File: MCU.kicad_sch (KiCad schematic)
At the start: 16 parts, among them SW1 KMR221NGLFS, U1 STM32L432KCUx

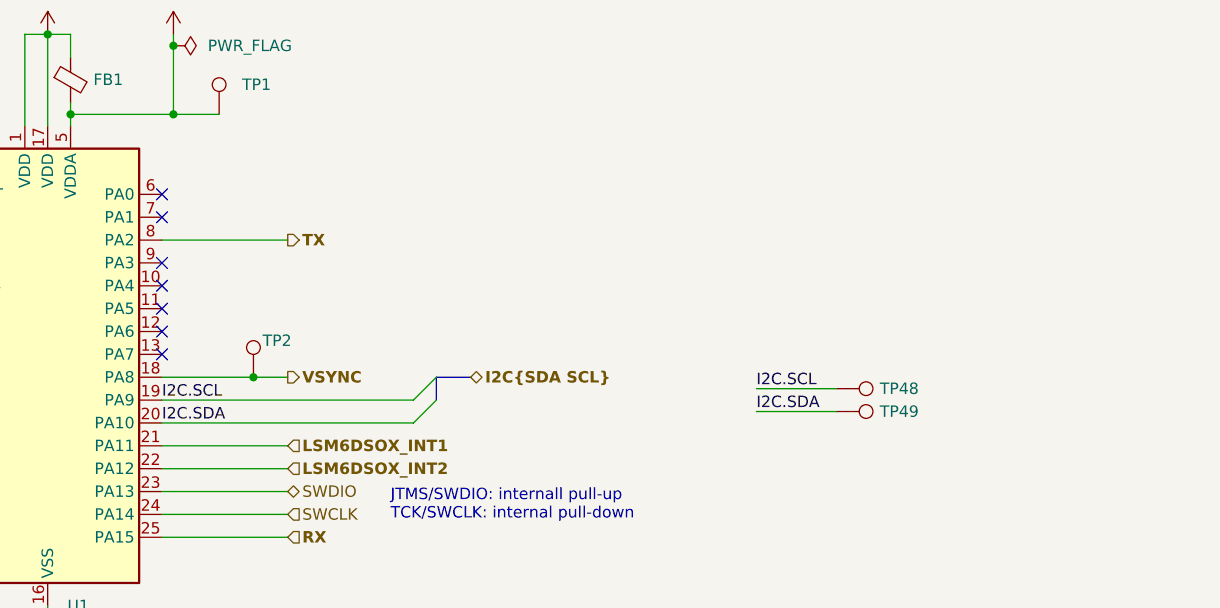
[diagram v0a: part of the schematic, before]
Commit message: Changed PUs for I2C and added TPs.
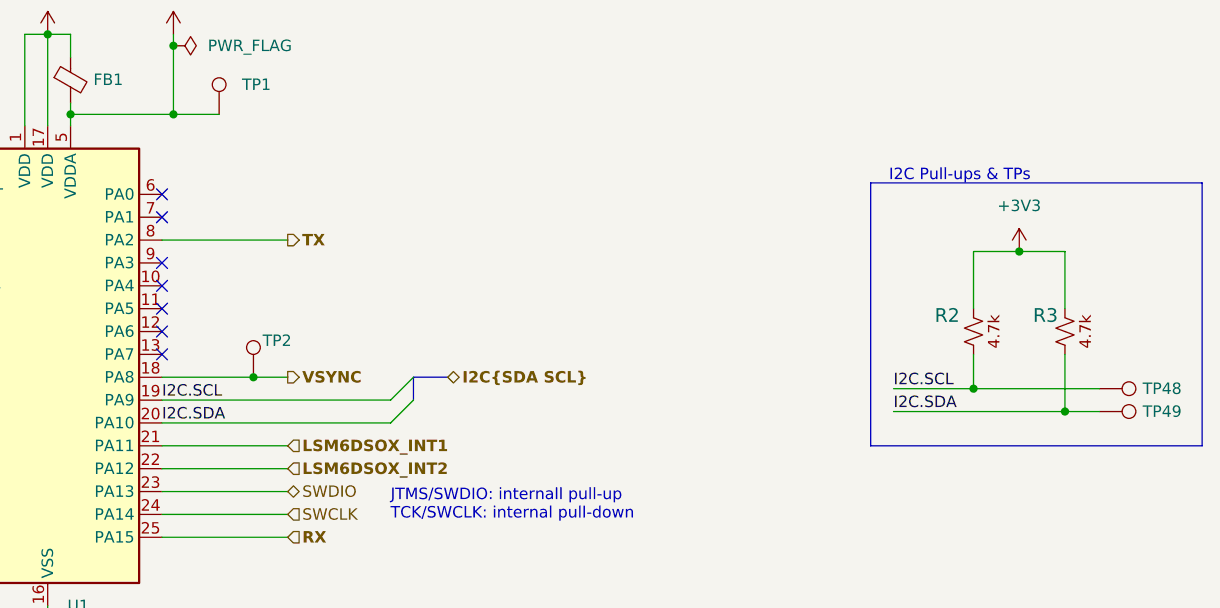
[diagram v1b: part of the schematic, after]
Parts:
- added R2, R3: CRGCQ0805F4K7, Hourglass_footprint_library:CRGCQ0805F4K7, symbol Hourglass_symbol_library:CRGCQ0805F4K7
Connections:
- net +3V3: now also R2.2, R3.2
- net I2C.SCL: now also R2.1
- net I2C.SDA: now also R3.1
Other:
- note added: "I2C Pull-ups & TPs"
- moved on the sheet: TP48, TP49

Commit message: Re-annotated entire schematic.
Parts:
- renumbered R17 to R1, R1 to R4, TP48 to TP3, TP49 to TP4, TP50 to TP5
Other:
- title: (none) -> Hourglass
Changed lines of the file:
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@@
 	(generator_version "9.0")
 	(paper "A4")
+	(title_block
+		(title "Hourglass")
+		(date "2025-04-23")
+		(rev "01")
+	)
 	(rectangle
 		(start 16.51 53.34)
@@
 		(on_board yes)
 		(dnp no)
-		(property "Reference" "TP48"
+		(property "Reference" "TP3"
 			(at 271.5261 88.9 90)
 			(effects
@@
 			(project "Hourglass_PCBA"
 				(path "/a75630d2-15a7-42bc-8ce0-7846cbd1da6b/c8d454a4-a64d-492c-9043-c9910b58426e"
-					(reference "TP48")
+					(reference "TP3")
 					(unit 1)
 				)
@@
 		(on_board yes)
 		(dnp no)
-		(property "Reference" "TP49"
+		(property "Reference" "TP4"
 			(at 271.5261 91.44 90)
 			(effects
@@
 			(project "Hourglass_PCBA"
 				(path "/a75630d2-15a7-42bc-8ce0-7846cbd1da6b/c8d454a4-a64d-492c-9043-c9910b58426e"
-					(reference "TP49")
+					(reference "TP4")
 					(unit 1)
 				)
@@
 		(dnp no)
 		(fields_autoplaced yes)
-		(property "Reference" "#PWR10"
+		(property "Reference" "#PWR011"
 			(at 149.86 129.54 0)
 			(effects
@@
 			(project ""
 				(path "/a75630d2-15a7-42bc-8ce0-7846cbd1da6b/c8d454a4-a64d-492c-9043-c9910b58426e"
-					(reference "#PWR10")
+					(reference "#PWR011")
 					(unit 1)
 				)
@@
 		(on_board yes)
 		(dnp no)
-		(property "Reference" "R17"
+		(property "Reference" "R1"
 			(at 60.452 66.0398 90)
 			(effects
@@
 			(project ""
 				(path "/a75630d2-15a7-42bc-8ce0-7846cbd1da6b/c8d454a4-a64d-492c-9043-c9910b58426e"
-					(reference "R17")
+					(reference "R1")
 					(unit 1)
 				)
@@
 		(dnp no)
 		(fields_autoplaced yes)
-		(property "Reference" "#PWR03"
+		(property "Reference" "#PWR07"
 			(at 66.04 66.04 0)
 			(effects
@@
 			(project ""
 				(path "/a75630d2-15a7-42bc-8ce0-7846cbd1da6b/c8d454a4-a64d-492c-9043-c9910b58426e"
-					(reference "#PWR03")
+					(reference "#PWR07")
 					(unit 1)
 				)
@@
 		(dnp no)
 		(fields_autoplaced yes)
-		(property "Reference" "#FLG3"
+		(property "Reference" "#FLG01"
 			(at 165.735 50.8 0)
 			(effects
@@
 			(project ""
 				(path "/a75630d2-15a7-42bc-8ce0-7846cbd1da6b/c8d454a4-a64d-492c-9043-c9910b58426e"
-					(reference "#FLG3")
+					(reference "#FLG01")
 					(unit 1)
 				)
@@
 		(on_board yes)
 		(dnp no)
-		(property "Reference" "R1"
+		(property "Reference" "R4"
 			(at 26.416 127.2538 90)
 			(effects
@@
 			(project ""
 				(path "/a75630d2-15a7-42bc-8ce0-7846cbd1da6b/c8d454a4-a64d-492c-9043-c9910b58426e"
-					(reference "R1")
+					(reference "R4")
 					(unit 1)
 				)
@@
 		(dnp no)
 		(fields_autoplaced yes)
-		(property "Reference" "#PWR5"
+		(property "Reference" "#PWR05"
 			(at 149.86 53.34 0)
 			(effects
@@
 			(project ""
 				(path "/a75630d2-15a7-42bc-8ce0-7846cbd1da6b/c8d454a4-a64d-492c-9043-c9910b58426e"
-					(reference "#PWR5")
+					(reference "#PWR05")
 					(unit 1)
 				)
@@
 		(dnp no)
 		(fields_autoplaced yes)
-		(property "Reference" "#PWR4"
+		(property "Reference" "#PWR03"
 			(at 190.5 44.45 0)
 			(effects
@@
 			(project ""
 				(path "/a75630d2-15a7-42bc-8ce0-7846cbd1da6b/c8d454a4-a64d-492c-9043-c9910b58426e"
-					(reference "#PWR4")
+					(reference "#PWR03")
 					(unit 1)
 				)
@@
 		(dnp no)
 		(fields_autoplaced yes)
-		(property "Reference" "#PWR020"
+		(property "Reference" "#PWR08"
 			(at 257.81 77.47 0)
 			(effects
@@
 			(project "Hourglass_PCBA"
 				(path "/a75630d2-15a7-42bc-8ce0-7846cbd1da6b/c8d454a4-a64d-492c-9043-c9910b58426e"
-					(reference "#PWR020")
+					(reference "#PWR08")
 					(unit 1)
 				)
@@
 		(dnp no)
 		(fields_autoplaced yes)
-		(property "Reference" "#PWR8"
+		(property "Reference" "#PWR010"
 			(at 66.04 88.9 0)
 			(effects
@@
 			(project ""
 				(path "/a75630d2-15a7-42bc-8ce0-7846cbd1da6b/c8d454a4-a64d-492c-9043-c9910b58426e"
-					(reference "#PWR8")
+					(reference "#PWR010")
 					(unit 1)
 				)
@@
 		(on_board yes)
 		(dnp no)
-		(property "Reference" "#PWR2"
+		(property "Reference" "#PWR02"
 			(at 190.5 27.94 0)
 			(effects
@@
 			(project "Hourglass_PCBA"
 				(path "/a75630d2-15a7-42bc-8ce0-7846cbd1da6b/c8d454a4-a64d-492c-9043-c9910b58426e"
-					(reference "#PWR2")
+					(reference "#PWR02")
 					(unit 1)
 				)
@@
 		(on_board yes)
 		(dnp no)
-		(property "Reference" "TP50"
+		(property "Reference" "TP5"
 			(at 124.206 91.1859 0)
 			(effects
@@
 			(project "Hourglass_PCBA"
 				(path "/a75630d2-15a7-42bc-8ce0-7846cbd1da6b/c8d454a4-a64d-492c-9043-c9910b58426e"
-					(reference "TP50")
+					(reference "TP5")
 					(unit 1)
 				)
@@
 		(dnp no)
 		(fields_autoplaced yes)
-		(property "Reference" "#PWR7"
+		(property "Reference" "#PWR09"
 			(at 22.86 88.9 0)
 			(effects
@@
 			(project ""
 				(path "/a75630d2-15a7-42bc-8ce0-7846cbd1da6b/c8d454a4-a64d-492c-9043-c9910b58426e"
-					(reference "#PWR7")
+					(reference "#PWR09")
 					(unit 1)
 				)
@@
 		(dnp no)
 		(fields_autoplaced yes)
-		(property "Reference" "#PWR1"
+		(property "Reference" "#PWR01"
 			(at 124.46 24.13 0)
 			(effects
@@
 			(project "Hourglass_PCBA"
 				(path "/a75630d2-15a7-42bc-8ce0-7846cbd1da6b/c8d454a4-a64d-492c-9043-c9910b58426e"
-					(reference "#PWR1")
+					(reference "#PWR01")
 					(unit 1)
 				)
@@
 		(dnp no)
 		(fields_autoplaced yes)
-		(property "Reference" "#PWR9"
+		(property "Reference" "#PWR012"
 			(at 30.48 142.24 0)
 			(effects
@@
 			(project ""
 				(path "/a75630d2-15a7-42bc-8ce0-7846cbd1da6b/c8d454a4-a64d-492c-9043-c9910b58426e"
-					(reference "#PWR9")
+					(reference "#PWR012")
 					(unit 1)
 				)
@@
 		(dnp no)
 		(fields_autoplaced yes)
-		(property "Reference" "#PWR6"
+		(property "Reference" "#PWR06"
 			(at 163.83 53.34 0)
 			(effects
@@
 			(project ""
 				(path "/a75630d2-15a7-42bc-8ce0-7846cbd1da6b/c8d454a4-a64d-492c-9043-c9910b58426e"
-					(reference "#PWR6")
+					(reference "#PWR06")
 					(unit 1)
 				)
@@
 		(dnp no)
 		(fields_autoplaced yes)
-		(property "Reference" "#PWR51"
+		(property "Reference" "#PWR04"
 			(at 124.46 49.53 0)
 			(effects
@@
 			(project "Hourglass_PCBA"
 				(path "/a75630d2-15a7-42bc-8ce0-7846cbd1da6b/c8d454a4-a64d-492c-9043-c9910b58426e"
-					(reference "#PWR51")
+					(reference "#PWR04")
 					(unit 1)
 				)

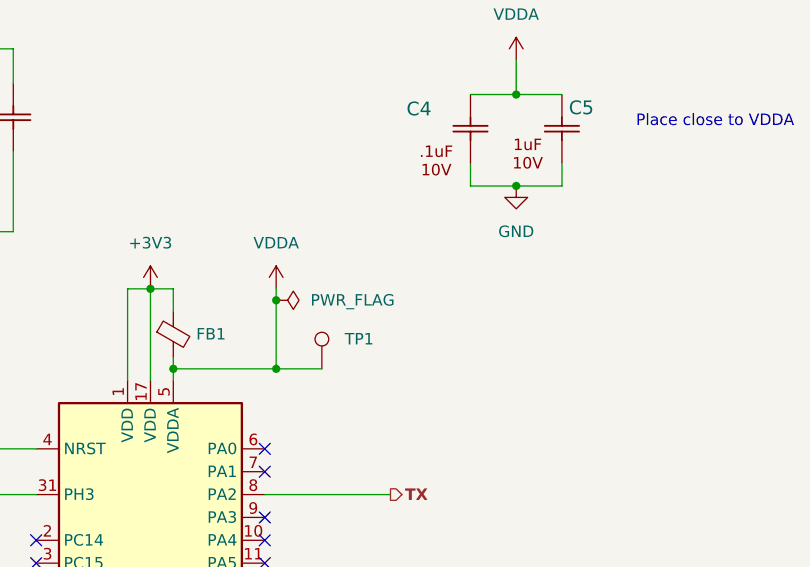
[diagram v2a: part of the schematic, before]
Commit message: Fixed ERC Errors.
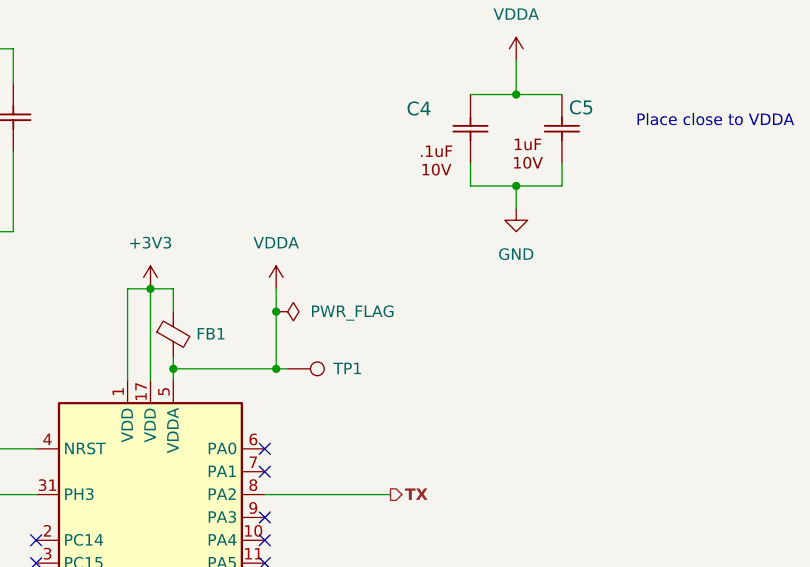
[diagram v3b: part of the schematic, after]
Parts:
- removed FB1: FCM 1608KF-601T03, Hourglass_footprint_library:FB_0603_1608Metric, symbol Hourglass_symbol_library:FerriteBead_Small
- added FB1: FCM 1608KF-601T03, Hourglass_footprint_library:FB_0603_1608Metric, symbol Hourglass_symbol_library:FCM 1608KF-601T03
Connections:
- net +3V3: now also FB1.1
- net VDDA: now also FB1.2
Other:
- moved on the sheet: TP1
